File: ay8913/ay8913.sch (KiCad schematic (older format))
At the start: 3 parts

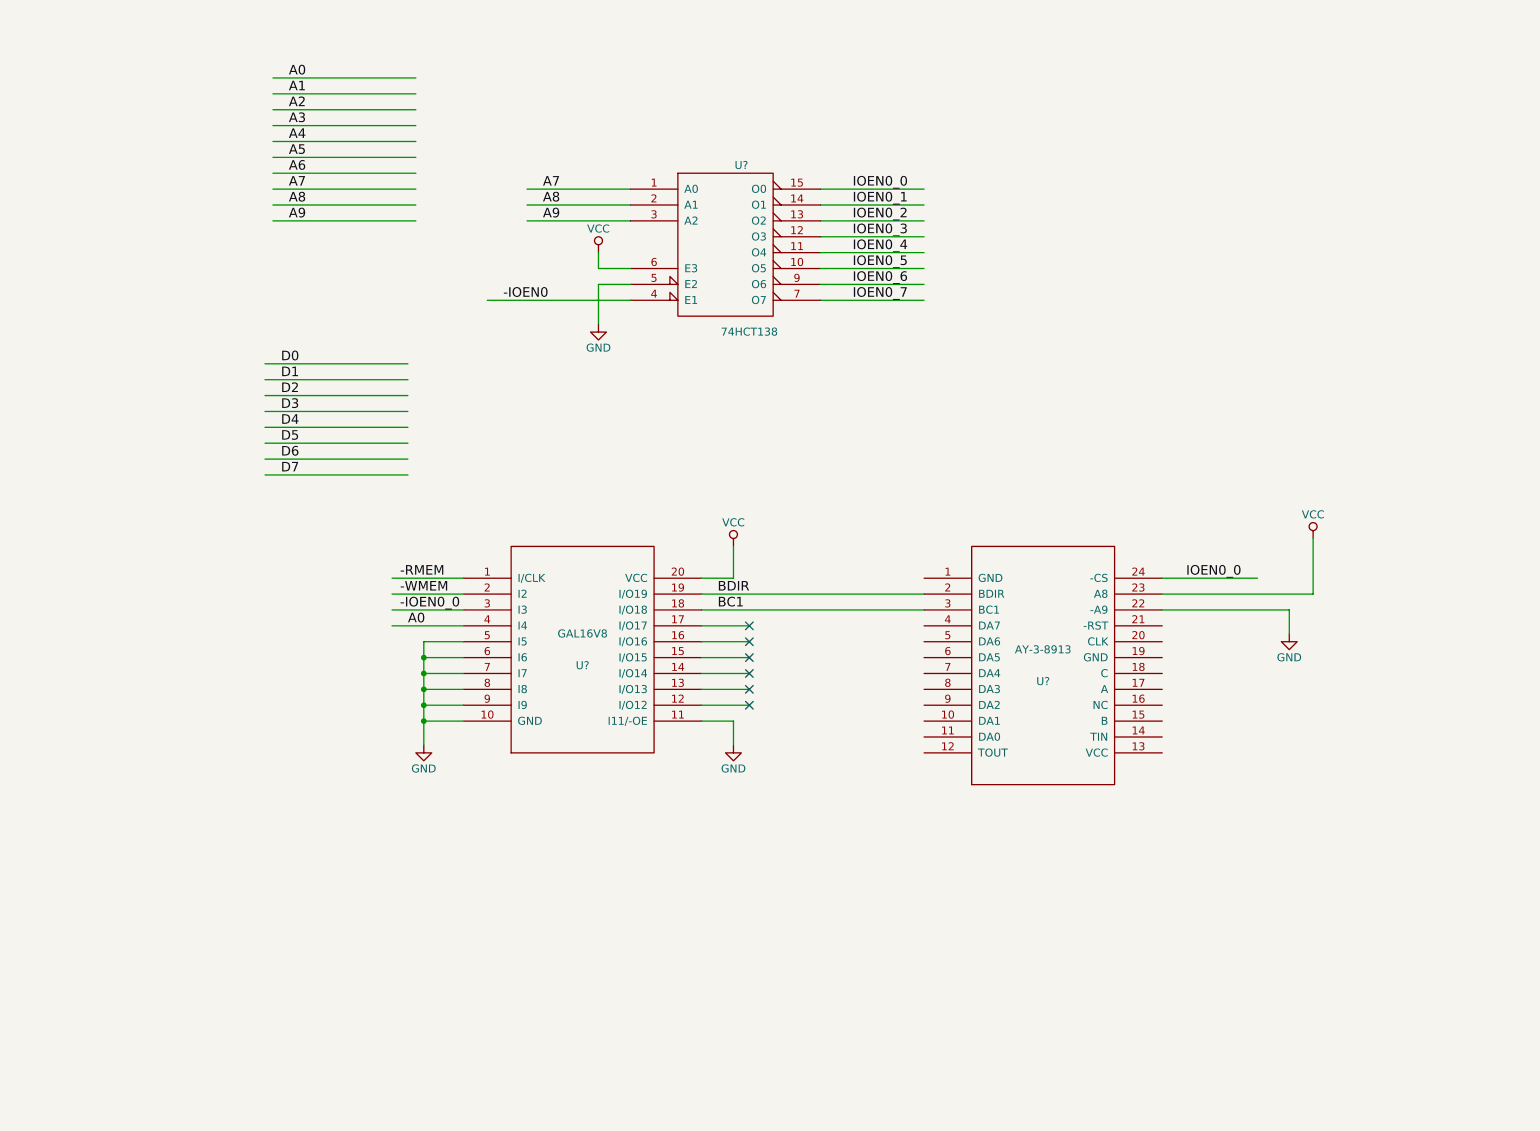
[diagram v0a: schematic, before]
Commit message: more work on AY-3-8913 circuit
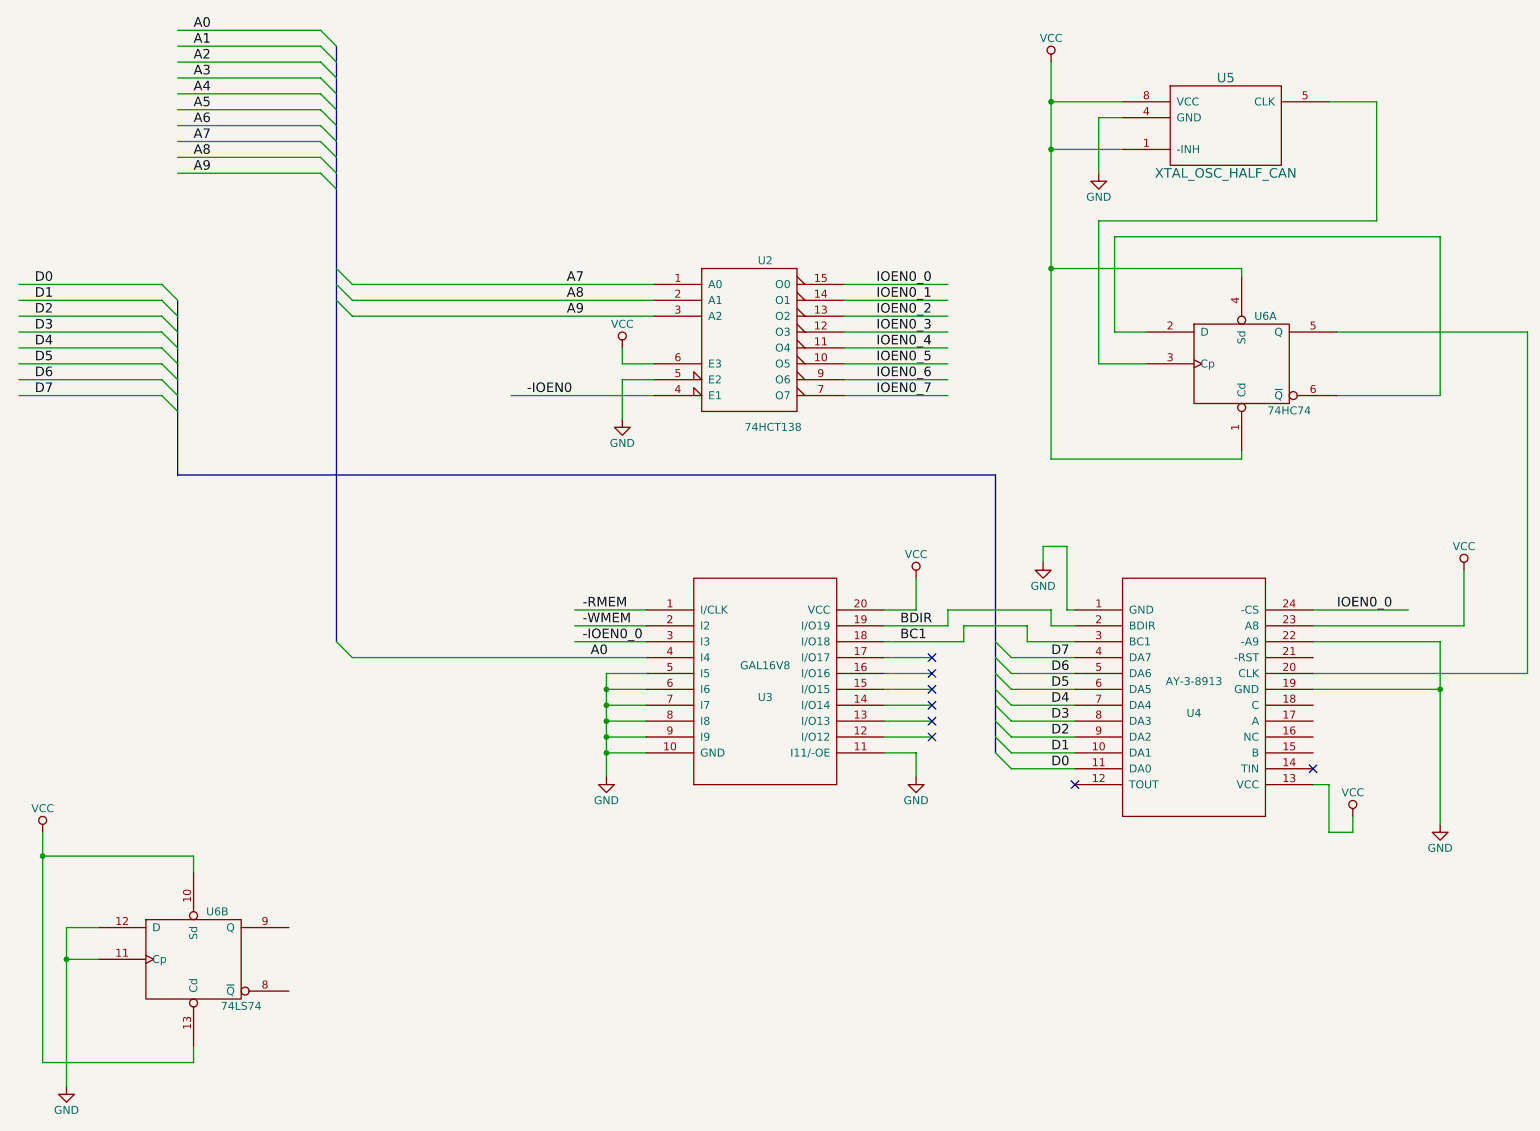
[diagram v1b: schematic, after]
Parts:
- added U5: XTAL_OSC_HALF_CAN, symbol XTAL_OSC_HALF_CAN
- added U6: 74HC74, symbol 74LS74
- gave numbers to parts that had none: 3
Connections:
- wire segments 67 -> 117
- no-connect marks 6 -> 8
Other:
- moved on the sheet: U2, U3, U4

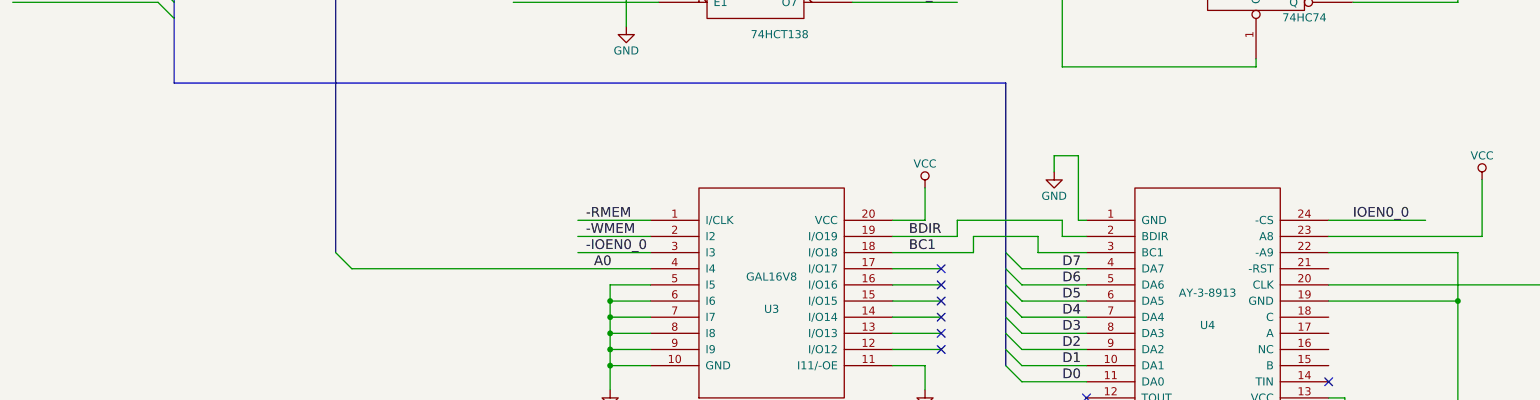
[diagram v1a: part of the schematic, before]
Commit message: use -RST signal
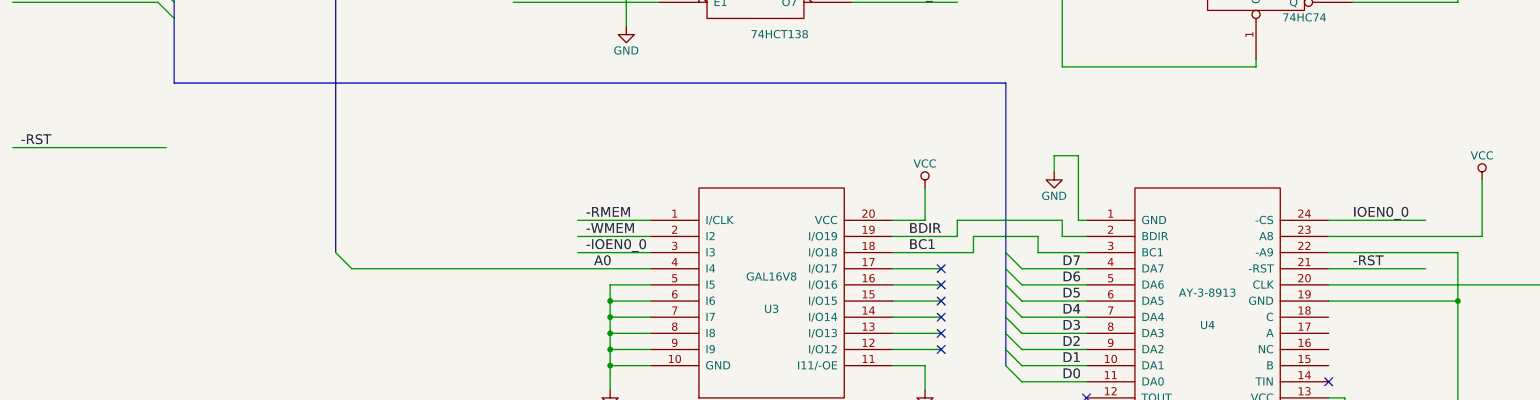
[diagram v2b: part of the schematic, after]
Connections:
- net labels added: -RST
- wire segments 117 -> 119
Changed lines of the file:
@@
 	1    0    0    -1
 $EndComp
+Wire Wire Line
+	800  3900 1750 3900
+Text Label 850  3900 0    60   ~ 0
+-RST
+Wire Wire Line
+	8950 4650 9550 4650
+Text Label 9100 4650 0    60   ~ 0
+-RST
 $EndSCHEMATC
